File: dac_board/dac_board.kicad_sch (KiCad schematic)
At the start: 0 parts

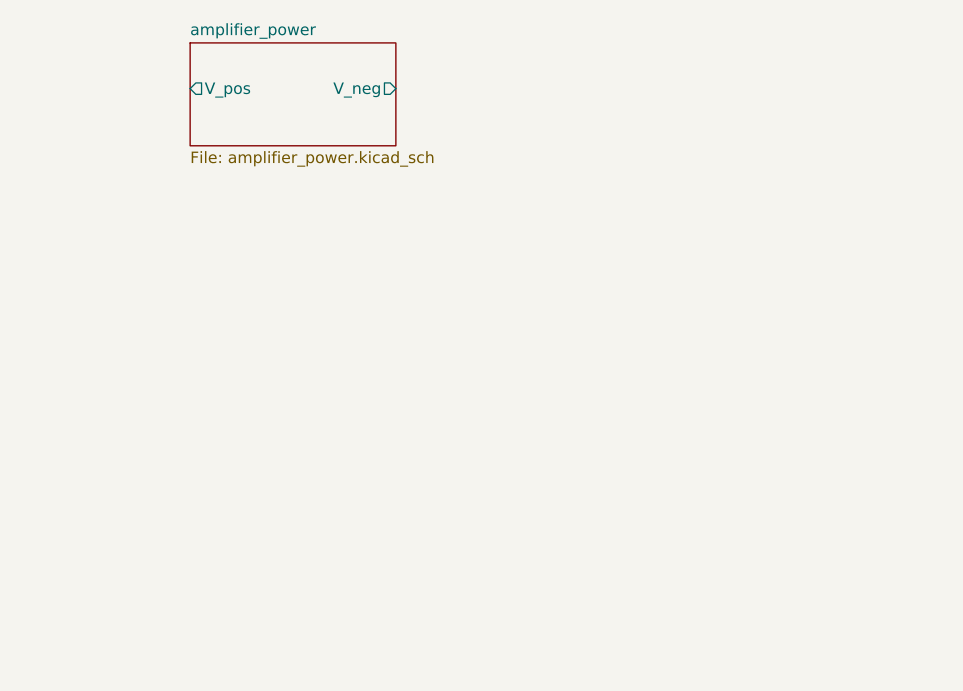
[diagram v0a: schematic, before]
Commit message: Finished adding everything with a SPICE simulation
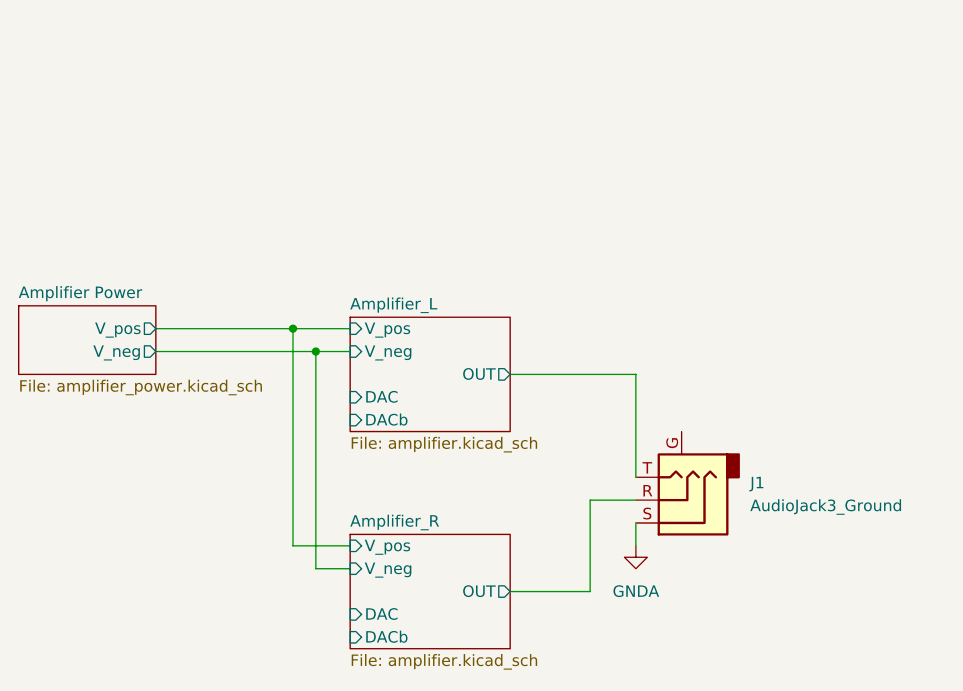
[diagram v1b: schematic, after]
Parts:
- added J1: AudioJack3_Ground, symbol Connector_Audio:AudioJack3_Ground
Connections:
- new net Amplifier_L/OUT: J1.T
- new net Amplifier_R/OUT: J1.R
- new net GNDA: J1.S
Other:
- sheet amplifier_power renamed Amplifier Power
- added sheet Amplifier_L (amplifier.kicad_sch)
- added sheet Amplifier_R (amplifier.kicad_sch)

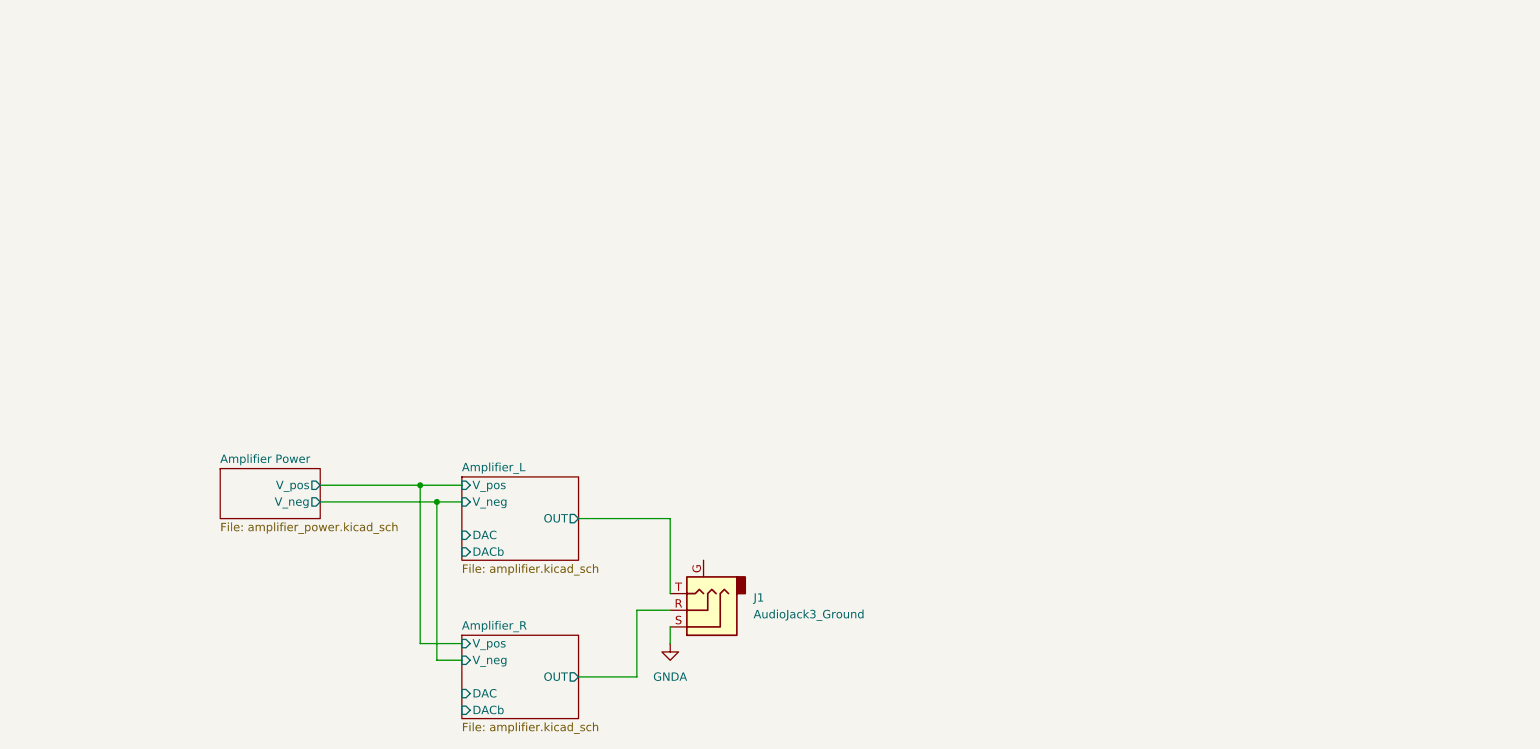
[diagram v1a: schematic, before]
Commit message: Additional work on DAC
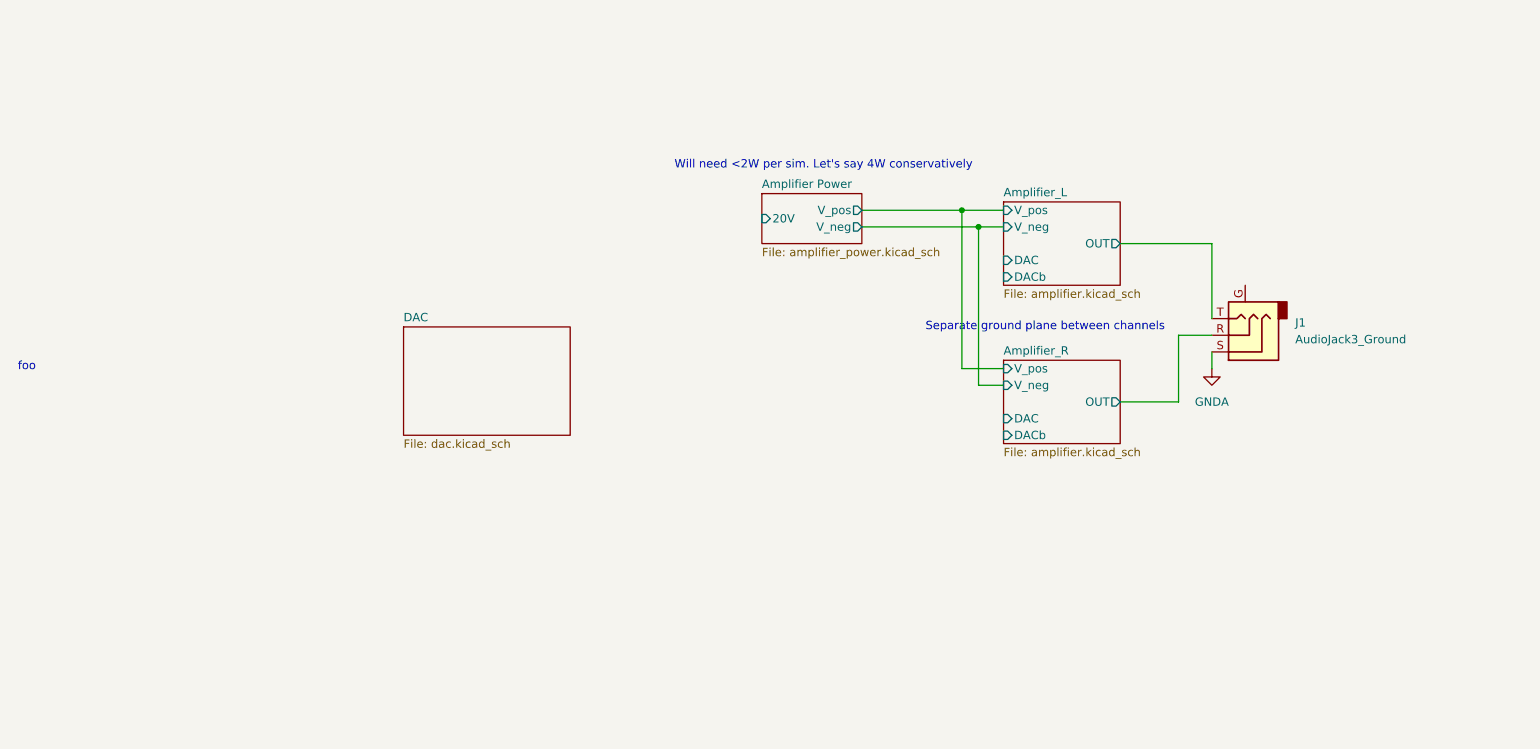
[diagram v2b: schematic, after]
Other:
- added sheet DAC (dac.kicad_sch)
- sheet Amplifier Power ports: added 20V; removed none
- note added: "Separate ground plane between channels"
- note added: "Will need <2W per sim. Let's say 4W conservatively"
- note added: "foo"
- moved on the sheet: J1

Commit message: More updates, finished DAC block
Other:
- sheet DAC ports: added APOWER_5V, DAC1, DAC1b, DAC2, DAC2b, I2C_SCL, I2C_SDA, I2S_BCLK, I2S_DATA, I2S_WS, MCLK, POWER3V3; removed none
- note removed: "foo"
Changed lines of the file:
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@@
-		)
-	)
-	(text "foo"
-		(exclude_from_sim no)
-		(at 49.276 97.536 0)
-		(effects
-			(font
-				(size 1.27 1.27)
-			)
 		)
 	)
@@
 	(wire
 		(pts
+			(xy 125.73 90.17) (xy 182.88 90.17)
+		)
+		(stroke
+			(width 0)
+			(type default)
+		)
+	)
+	(wire
+		(pts
 			(xy 215.9 78.74) (xy 229.87 78.74)
 		)
@@
 	(wire
 		(pts
+			(xy 185.42 83.82) (xy 198.12 83.82)
+		)
+		(stroke
+			(width 0)
+			(type default)
+		)
+	)
+	(wire
+		(pts
 			(xy 191.77 97.79) (xy 198.12 97.79)
 		)
@@
 	(wire
 		(pts
+			(xy 125.73 97.79) (xy 182.88 97.79)
+		)
+		(stroke
+			(width 0)
+			(type default)
+		)
+	)
+	(wire
+		(pts
+			(xy 182.88 81.28) (xy 198.12 81.28)
+		)
+		(stroke
+			(width 0)
+			(type default)
+		)
+	)
+	(wire
+		(pts
 			(xy 194.31 100.33) (xy 198.12 100.33)
 		)
@@
 	(wire
 		(pts
+			(xy 185.42 105.41) (xy 198.12 105.41)
+		)
+		(stroke
+			(width 0)
+			(type default)
+		)
+	)
+	(wire
+		(pts
+			(xy 185.42 92.71) (xy 185.42 83.82)
+		)
+		(stroke
+			(width 0)
+			(type default)
+		)
+	)
+	(wire
+		(pts
+			(xy 125.73 92.71) (xy 185.42 92.71)
+		)
+		(stroke
+			(width 0)
+			(type default)
+		)
+	)
+	(wire
+		(pts
 			(xy 224.79 92.71) (xy 229.87 92.71)
 		)
@@
 	(wire
 		(pts
+			(xy 185.42 95.25) (xy 185.42 105.41)
+		)
+		(stroke
+			(width 0)
+			(type default)
+		)
+	)
+	(wire
+		(pts
 			(xy 229.87 78.74) (xy 229.87 90.17)
 		)
@@
 	(wire
 		(pts
+			(xy 182.88 97.79) (xy 182.88 107.95)
+		)
+		(stroke
+			(width 0)
+			(type default)
+		)
+	)
+	(wire
+		(pts
 			(xy 194.31 76.2) (xy 194.31 100.33)
 		)
@@
 		(pts
 			(xy 176.53 73.66) (xy 191.77 73.66)
+		)
+		(stroke
+			(width 0)
+			(type default)
+		)
+	)
+	(wire
+		(pts
+			(xy 182.88 90.17) (xy 182.88 81.28)
+		)
+		(stroke
+			(width 0)
+			(type default)
+		)
+	)
+	(wire
+		(pts
+			(xy 125.73 95.25) (xy 185.42 95.25)
+		)
+		(stroke
+			(width 0)
+			(type default)
+		)
+	)
+	(wire
+		(pts
+			(xy 182.88 107.95) (xy 198.12 107.95)
 		)
 		(stroke
@@
 	)
 	(sheet
-		(at 106.68 91.44)
-		(size 25.4 16.51)
+		(at 87.63 85.09)
+		(size 38.1 20.32)
 		(exclude_from_sim no)
 		(in_bom yes)
@@
 		)
 		(property "Sheetname" "DAC"
-			(at 106.68 90.7284 0)
+			(at 87.63 84.3784 0)
 			(effects
 				(font
@@
 		)
 		(property "Sheetfile" "dac.kicad_sch"
-			(at 106.68 108.5346 0)
+			(at 87.63 105.9946 0)
 			(effects
 				(font
@@
 			)
 		)
+		(pin "APOWER_5V" input
+			(at 87.63 93.98 180)
+			(effects
+				(font
+					(size 1.27 1.27)
+				)
+				(justify left)
+			)
+		)
+		(pin "DAC1" output
+			(at 125.73 90.17 0)
+			(effects
+				(font
+					(size 1.27 1.27)
+				)
+				(justify right)
+			)
+		)
+		(pin "DAC1b" output
+			(at 125.73 92.71 0)
+			(effects
+				(font
+					(size 1.27 1.27)
+				)
+				(justify right)
+			)
+		)
+		(pin "DAC2" output
+			(at 125.73 95.25 0)
+			(effects
+				(font
+					(size 1.27 1.27)
+				)
+				(justify right)
+			)
+		)
+		(pin "DAC2b" output
+			(at 125.73 97.79 0)
+			(effects
+				(font
+					(size 1.27 1.27)
+				)
+				(justify right)
+			)
+		)
+		(pin "I2C_SCL" input
+			(at 113.03 85.09 90)
+			(effects
+				(font
+					(size 1.27 1.27)
+				)
+				(justify right)
+			)
+		)
+		(pin "I2C_SDA" bidirectional
+			(at 115.57 85.09 90)
+			(effects
+				(font
+					(size 1.27 1.27)
+				)
+				(justify right)
+			)
+		)
+		(pin "I2S_BCLK" output
+			(at 110.49 85.09 90)
+			(effects
+				(font
+					(size 1.27 1.27)
+				)
+				(justify right)
+			)
+		)
+		(pin "I2S_DATA" input
+			(at 104.14 85.09 90)
+			(effects
+				(font
+					(size 1.27 1.27)
+				)
+				(justify right)
+			)
+		)
+		(pin "I2S_WS" output
+			(at 101.6 85.09 90)
+			(effects
+				(font
+					(size 1.27 1.27)
+				)
+				(justify right)
+			)
+		)
+		(pin "MCLK" input
+			(at 109.22 105.41 270)
+			(effects
+				(font
+					(size 1.27 1.27)
+				)
+				(justify left)
+			)
+		)
+		(pin "POWER3V3" input
+			(at 87.63 96.52 180)
+			(effects
+				(font
+					(size 1.27 1.27)
+				)
+				(justify left)
+			)
+		)

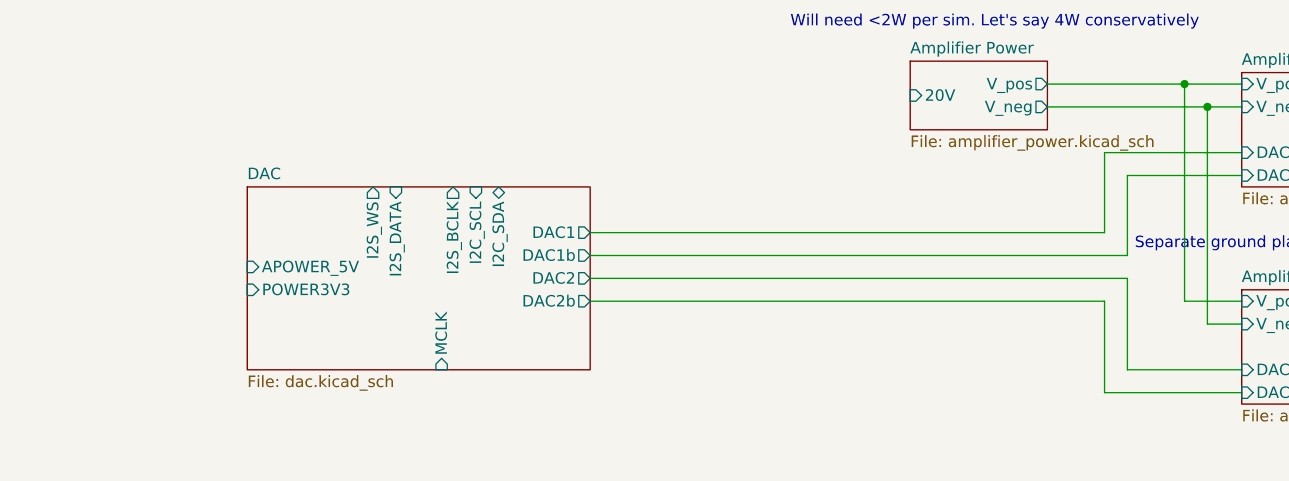
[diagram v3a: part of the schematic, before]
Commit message: Added MCU and associated logic
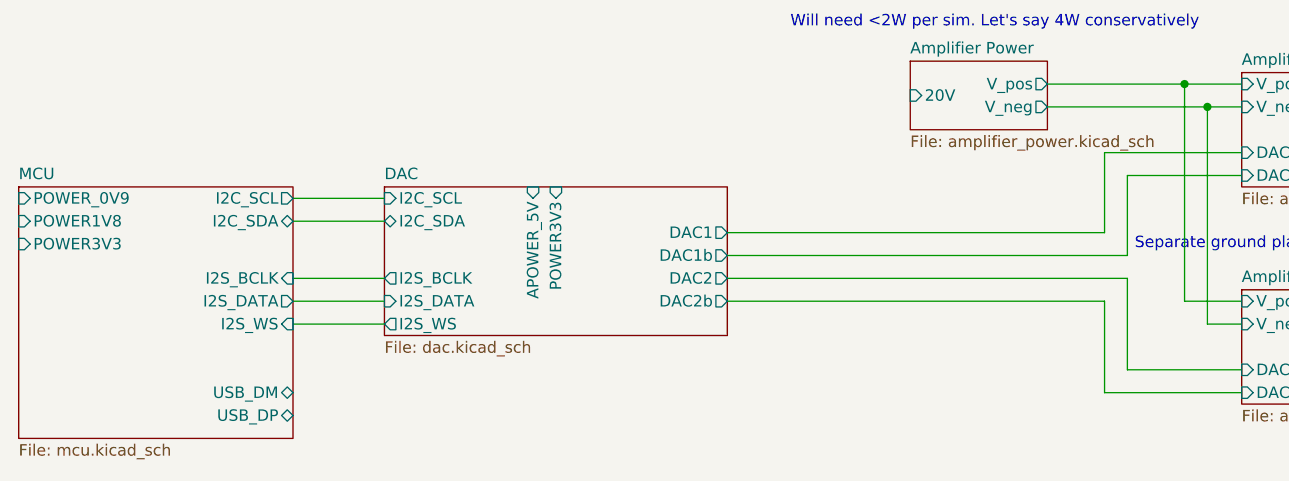
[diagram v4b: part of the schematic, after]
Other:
- added sheet MCU (mcu.kicad_sch)
- sheet DAC ports: added none; removed MCLK
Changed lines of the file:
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@@
 	(wire
 		(pts
-			(xy 125.73 90.17) (xy 182.88 90.17)
+			(xy 140.97 90.17) (xy 182.88 90.17)
 		)
 		(stroke
@@
 	(wire
 		(pts
-			(xy 125.73 97.79) (xy 182.88 97.79)
+			(xy 140.97 97.79) (xy 182.88 97.79)
+		)
+		(stroke
+			(width 0)
+			(type default)
+		)
+	)
+	(wire
+		(pts
+			(xy 92.71 95.25) (xy 102.87 95.25)
 		)
 		(stroke
@@
 	(wire
 		(pts
+			(xy 92.71 100.33) (xy 102.87 100.33)
+		)
+		(stroke
+			(width 0)
+			(type default)
+		)
+	)
+	(wire
+		(pts
 			(xy 194.31 100.33) (xy 198.12 100.33)
 		)
@@
 	(wire
 		(pts
+			(xy 92.71 97.79) (xy 102.87 97.79)
+		)
+		(stroke
+			(width 0)
+			(type default)
+		)
+	)
+	(wire
+		(pts
 			(xy 176.53 76.2) (xy 194.31 76.2)
 		)
@@
 	(wire
 		(pts
-			(xy 125.73 92.71) (xy 185.42 92.71)
+			(xy 92.71 86.36) (xy 102.87 86.36)
+		)
+		(stroke
+			(width 0)
+			(type default)
+		)
+	)
+	(wire
+		(pts
+			(xy 140.97 92.71) (xy 185.42 92.71)
 		)
 		(stroke
@@
 	(wire
 		(pts
+			(xy 92.71 88.9) (xy 102.87 88.9)
+		)
+		(stroke
+			(width 0)
+			(type default)
+		)
+	)
+	(wire
+		(pts
 			(xy 182.88 90.17) (xy 182.88 81.28)
 		)
@@
 	(wire
 		(pts
-			(xy 125.73 95.25) (xy 185.42 95.25)
+			(xy 140.97 95.25) (xy 185.42 95.25)
 		)
 		(stroke
@@
 	)
 	(sheet
-		(at 87.63 85.09)
-		(size 38.1 20.32)
+		(at 62.23 85.09)
+		(size 30.48 27.94)
 		(exclude_from_sim no)
 		(in_bom yes)
@@
 			(color 0 0 0 0.0000)
 		)
+		(property "Sheetname" "MCU"
+			(at 62.23 84.3784 0)
+			(effects
+				(font
+					(size 1.27 1.27)
+				)
+				(justify left bottom)
+			)
+		)
+		(property "Sheetfile" "mcu.kicad_sch"
+			(at 62.23 113.6146 0)
+			(effects
+				(font
+					(size 1.27 1.27)
+				)
+				(justify left top)
+			)
+		)
+		(pin "I2C_SCL" output
+			(at 92.71 86.36 0)
+			(effects
+				(font
+					(size 1.27 1.27)
+				)
+				(justify right)
+			)
+		)
+		(pin "I2C_SDA" bidirectional
+			(at 92.71 88.9 0)
+			(effects
+				(font
+					(size 1.27 1.27)
+				)
+				(justify right)
+			)
+		)
+		(pin "I2S_BCLK" input
+			(at 92.71 95.25 0)
+			(effects
+				(font
+					(size 1.27 1.27)
+				)
+				(justify right)
+			)
+		)
+		(pin "I2S_DATA" output
+			(at 92.71 97.79 0)
+			(effects
+				(font
+					(size 1.27 1.27)
+				)
+				(justify right)
+			)
+		)
+		(pin "I2S_WS" input
+			(at 92.71 100.33 0)
+			(effects
+				(font
+					(size 1.27 1.27)
+				)
+				(justify right)
+			)
+		)
+		(pin "POWER1V8" input
+			(at 62.23 88.9 180)
+			(effects
+				(font
+					(size 1.27 1.27)
+				)
+				(justify left)
+			)
+		)
+		(pin "POWER3V3" input
+			(at 62.23 91.44 180)
+			(effects
+				(font
+					(size 1.27 1.27)
+				)
+				(justify left)
+			)
+		)
+		(pin "POWER_0V9" input
+			(at 62.23 86.36 180)
+			(effects
+				(font
+					(size 1.27 1.27)
+				)
+				(justify left)
+			)
+		)
+		(pin "USB_DM" bidirectional
+			(at 92.71 107.95 0)
+			(effects
+				(font
+					(size 1.27 1.27)
+				)
+				(justify right)
+			)
+		)
+		(pin "USB_DP" bidirectional
+			(at 92.71 110.49 0)
+			(effects
+				(font
+					(size 1.27 1.27)
+				)
+				(justify right)
+			)
+		)
+		(instances
+			(project "dac_board"
+				(path "/387b6079-e547-4b62-84b5-51a54c04db0a"
+					(page "6")
+				)
+			)
+		)
+	)
+	(sheet
+		(at 102.87 85.09)
+		(size 38.1 16.51)
+		(exclude_from_sim no)
+		(in_bom yes)
+		(on_board yes)
+		(dnp no)
+		(fields_autoplaced yes)
+		(stroke
+			(width 0.1524)
+			(type solid)
+		)
+		(fill
+			(color 0 0 0 0.0000)
+		)
 		(property "Sheetname" "DAC"
-			(at 87.63 84.3784 0)
+			(at 102.87 84.3784 0)
 			(effects
 				(font
@@
 		)
 		(property "Sheetfile" "dac.kicad_sch"
-			(at 87.63 105.9946 0)
+			(at 102.87 102.1846 0)
 			(effects
 				(font
@@
 		)
 		(pin "APOWER_5V" input
-			(at 87.63 93.98 180)
-			(effects
-				(font
-					(size 1.27 1.27)
-				)
-				(justify left)
+			(at 119.38 85.09 90)
+			(effects
+				(font
+					(size 1.27 1.27)
+				)
+				(justify right)
 			)
 		)
 		(pin "DAC1" output
-			(at 125.73 90.17 0)
+			(at 140.97 90.17 0)
 			(effects
 				(font
@@
 		)
 		(pin "DAC1b" output
-			(at 125.73 92.71 0)
+			(at 140.97 92.71 0)
 			(effects
 				(font
@@
 		)
 		(pin "DAC2" output
-			(at 125.73 95.25 0)
+			(at 140.97 95.25 0)
 			(effects
 				(font
@@
 		)
 		(pin "DAC2b" output
-			(at 125.73 97.79 0)
+			(at 140.97 97.79 0)
 			(effects
 				(font
@@
 		)
 		(pin "I2C_SCL" input
-			(at 113.03 85.09 90)
-			(effects
-				(font
-					(size 1.27 1.27)
-				)
-				(justify right)
+			(at 102.87 86.36 180)
+			(effects
+				(font
+					(size 1.27 1.27)
+				)
+				(justify left)
 			)
 		)
 		(pin "I2C_SDA" bidirectional
-			(at 115.57 85.09 90)
-			(effects
-				(font
-					(size 1.27 1.27)
-				)
-				(justify right)
+			(at 102.87 88.9 180)
+			(effects
+				(font
+					(size 1.27 1.27)
+				)
+				(justify left)
 			)
 		)
 		(pin "I2S_BCLK" output
-			(at 110.49 85.09 90)
-			(effects
-				(font
-					(size 1.27 1.27)
-				)
-				(justify right)
+			(at 102.87 95.25 180)
+			(effects
+				(font
+					(size 1.27 1.27)
+				)
+				(justify left)
 			)
 		)
 		(pin "I2S_DATA" input
-			(at 104.14 85.09 90)
-			(effects
-				(font
-					(size 1.27 1.27)
-				)
-				(justify right)
+			(at 102.87 97.79 180)
+			(effects
+				(font
+					(size 1.27 1.27)
+				)
+				(justify left)
 			)
 		)
 		(pin "I2S_WS" output
-			(at 101.6 85.09 90)
-			(effects
-				(font
-					(size 1.27 1.27)
-				)
-				(justify right)
-			)
-		)
-		(pin "MCLK" input
-			(at 109.22 105.41 270)
+			(at 102.87 100.33 180)
 			(effects
 				(font
@@
 		)
 		(pin "POWER3V3" input
-			(at 87.63 96.52 180)
-			(effects
-				(font
-					(size 1.27 1.27)
-				)
-				(justify left)
-			)
-		)
+			(at 121.92 85.09 90)
+			(effects
+				(font
+					(size 1.27 1.27)
+				)
+				(justify right)
+			)
+		)
